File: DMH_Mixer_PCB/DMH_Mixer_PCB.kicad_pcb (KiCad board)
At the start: 2 copper layers, 48 x 138 mm, 41 parts, among them J0 Conn_01x01, J100 IDC_02x05, J200 IDC_02x05, J50 Conn_01x08, J60 Conn_01x08, SW1 SW_SPDT_321, SW2 SW_SPDT_321, SW3 SW_SPDT_321, SW4 SW_SPDT_321, U1 TL074

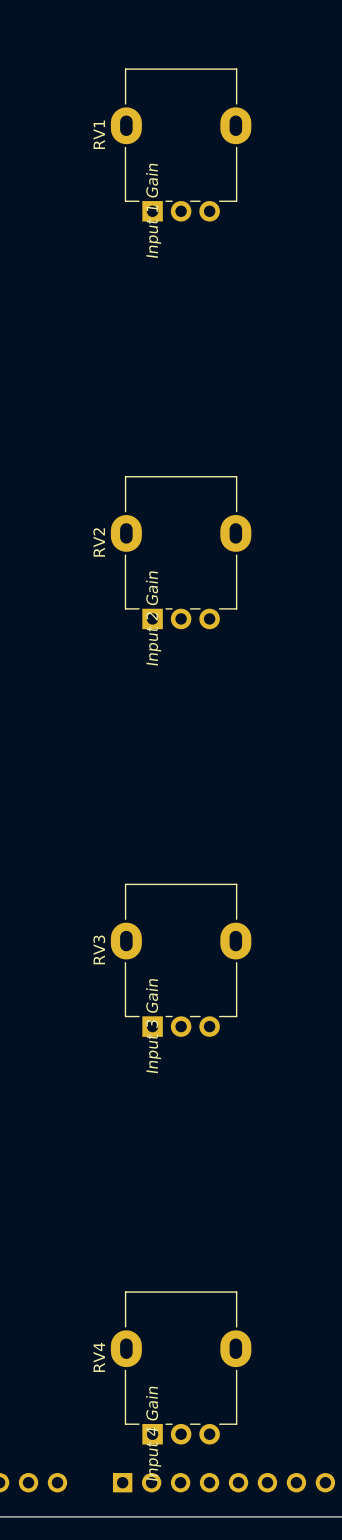
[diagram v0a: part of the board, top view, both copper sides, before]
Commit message: Moved pots to X=83,25
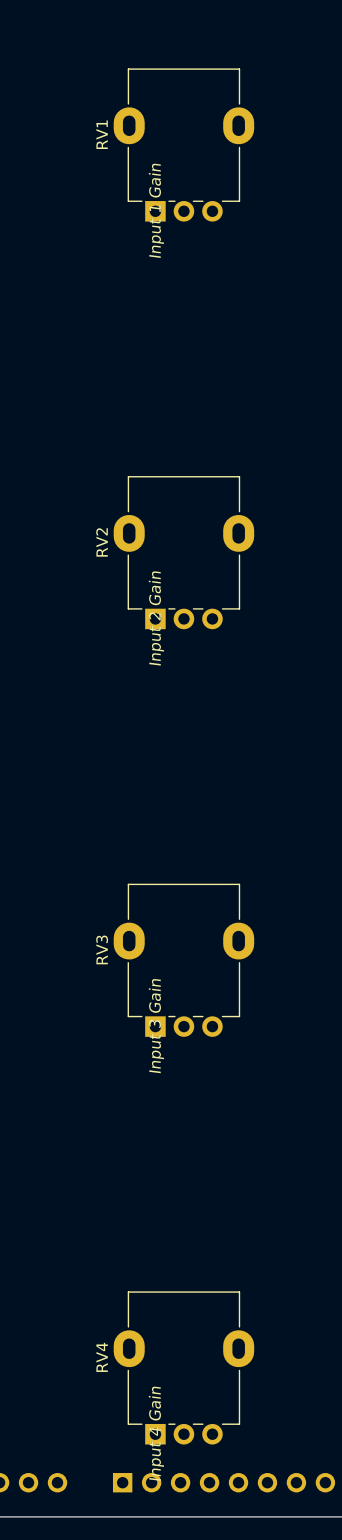
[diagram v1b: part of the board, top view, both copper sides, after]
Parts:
- moved RV1 0.25 mm to (80.8, 66.0)
- moved RV2 0.25 mm to (80.8, 101.8)
- moved RV3 0.25 mm to (80.8, 137.5)
- moved RV4 0.25 mm to (80.8, 173.2)
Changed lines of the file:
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@@
 	(footprint "SynthStuff:Potentiometer_Alpha_RD901F-40-00D_Single_Vertical"
 		(layer "F.Cu")
-		(at 80.5 173.25 90)
+		(at 80.75 173.25 90)
 		(descr "Potentiometer, vertical, 9mm, single, http://www.taiwanalpha.com.tw/downloads?target=products&id=113")
 		(tags "potentiometer vertical 9mm single")
@@
 	(footprint "SynthStuff:Potentiometer_Alpha_RD901F-40-00D_Single_Vertical"
 		(layer "F.Cu")
-		(at 80.5 101.75 90)
+		(at 80.75 101.75 90)
 		(descr "Potentiometer, vertical, 9mm, single, http://www.taiwanalpha.com.tw/downloads?target=products&id=113")
 		(tags "potentiometer vertical 9mm single")
@@
 	(footprint "SynthStuff:Potentiometer_Alpha_RD901F-40-00D_Single_Vertical"
 		(layer "F.Cu")
-		(at 80.5 137.5 90)
+		(at 80.75 137.5 90)
 		(descr "Potentiometer, vertical, 9mm, single, http://www.taiwanalpha.com.tw/downloads?target=products&id=113")
 		(tags "potentiometer vertical 9mm single")
@@
 	(footprint "SynthStuff:Potentiometer_Alpha_RD901F-40-00D_Single_Vertical"
 		(layer "F.Cu")
-		(at 80.5 66 90)
+		(at 80.75 66 90)
 		(descr "Potentiometer, vertical, 9mm, single, http://www.taiwanalpha.com.tw/downloads?target=products&id=113")
 		(tags "potentiometer vertical 9mm single")
@@
 	)
 	(gr_line
-		(start 83 169.25)
-		(end 83 162.25)
-		(stroke
-			(width 0.1)
-			(type default)
-		)
-		(layer "Cmts.User")
-	)
-	(gr_line
-		(start 79.5 58.5)
-		(end 86.5 58.5)
+		(start 83.25 169.25)
+		(end 83.25 162.25)
 		(stroke
 			(width 0.1)
@@
 	)
 	(gr_line
-		(start 79.5 94.25)
-		(end 86.5 94.25)
-		(stroke
-			(width 0.1)
-			(type default)
-		)
-		(layer "Cmts.User")
-	)
-	(gr_line
-		(start 83 62)
-		(end 83 55)
+		(start 79.75 94.25)
+		(end 86.75 94.25)
 		(stroke
 			(width 0.1)
@@
 	)
 	(gr_circle
-		(center 83 165.75)
-		(end 83 169.25)
+		(center 83.25 165.75)
+		(end 83.25 169.25)
 		(stroke
 			(width 0.1)
@@
 	)
 	(gr_line
-		(start 79.5 165.75)
-		(end 86.5 165.75)
+		(start 79.75 165.75)
+		(end 86.75 165.75)
 		(stroke
 			(width 0.1)
@@
 	)
 	(gr_line
-		(start 79.5 130)
-		(end 86.5 130)
+		(start 79.75 130)
+		(end 86.75 130)
 		(stroke
 			(width 0.1)
@@
 		(layer "Cmts.User")
 	)
+	(gr_line
+		(start 79.75 58.5)
+		(end 86.75 58.5)
+		(stroke
+			(width 0.1)
+			(type default)
+		)
+		(layer "Cmts.User")
+	)
 	(gr_circle
-		(center 83 130)
-		(end 83 133.5)
+		(center 83.25 130)
+		(end 83.25 133.5)
 		(stroke
 			(width 0.1)
@@
 	)
 	(gr_circle
-		(center 83 58.5)
-		(end 83 62)
+		(center 83.25 58.5)
+		(end 83.25 62)
 		(stroke
 			(width 0.1)
@@
 	)
 	(gr_line
-		(start 83 97.75)
-		(end 83 90.75)
+		(start 83.25 97.75)
+		(end 83.25 90.75)
 		(stroke
 			(width 0.1)
@@
 	)
 	(gr_circle
-		(center 83 94.25)
-		(end 83 97.75)
+		(center 83.25 94.25)
+		(end 83.25 97.75)
 		(stroke
 			(width 0.1)
@@
 	)
 	(gr_line
-		(start 83 133.5)
-		(end 83 126.5)
+		(start 83.25 62)
+		(end 83.25 55)
+		(stroke
+			(width 0.1)
+			(type default)
+		)
+		(layer "Cmts.User")
+	)
+	(gr_line
+		(start 83.25 133.5)
+		(end 83.25 126.5)
 		(stroke
 			(width 0.1)

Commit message: Component placement done
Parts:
- added C10: 1uF, Capacitor_THT:C_Disc_D4.3mm_W1.9mm_P5.00mm, B.Cu at (53.0, 158.5)
- added C7: 1uF, Capacitor_THT:C_Disc_D4.3mm_W1.9mm_P5.00mm, B.Cu at (53.0, 51.0)
- added C8: 1uF, Capacitor_THT:C_Disc_D4.3mm_W1.9mm_P5.00mm, B.Cu at (53.0, 86.8)
- added C9: 1uF, Capacitor_THT:C_Disc_D4.3mm_W1.9mm_P5.00mm, B.Cu at (53.0, 124.0)
- added R17: 100k, Resistor_THT:R_Axial_DIN0207_L6.3mm_D2.5mm_P7.62mm_Horizontal, B.Cu at (53.0, 65.8)
- added R18: 27k, Resistor_THT:R_Axial_DIN0207_L6.3mm_D2.5mm_P7.62mm_Horizontal, B.Cu at (53.0, 93.9)
- added R19: 100k, Resistor_THT:R_Axial_DIN0207_L6.3mm_D2.5mm_P7.62mm_Horizontal, B.Cu at (53.0, 138.8)
- added R20: 1k, Resistor_THT:R_Axial_DIN0207_L6.3mm_D2.5mm_P7.62mm_Horizontal, B.Cu at (53.0, 173.3)
- C1, C2, C3, C4, C5, C6, D1, D2, D4, D5, J100, J200, R1, R10, R3, R5, R9, U1: moved to B.Cu
- R11: value 27k -> 100k; moved to B.Cu
- R12, R7: value 1k -> 100k; moved to B.Cu
- R13, R14, R15: value 33k -> 100k; moved to B.Cu
- R16: value 33k -> 1k; moved to B.Cu
- R2, R4, R6, R8: value 100k -> 27k; moved to B.Cu
- moved J0 137.0 mm to (56.2, 155.2)
- moved SW4 123.5 mm to (58.5, 165.8)
- moved C1 119.8 mm to (73.0, 47.2), turned to 180 degrees
- moved D5 106.1 mm to (77.4, 46.0)
- moved J200 105.3 mm to (70.3, 158.3), turned to 180 degrees
- moved C3 103.6 mm to (72.9, 110.2), turned to -90 degrees
- moved C4 102.7 mm to (82.1, 50.6), turned to 180 degrees
- moved RV5 100.6 mm to (53.9, 113.5), turned to 90 degrees
- moved SW3 97.1 mm to (58.5, 130.0)
- moved C2 90.8 mm to (94.5, 82.2)
- moved D1 89.4 mm to (59.4, 109.5)
- moved C5 85.8 mm to (91.2, 78.7), turned to 90 degrees
- moved D2 81.5 mm to (67.1, 115.2), turned to 180 degrees
- moved D4 81.2 mm to (95.8, 65.9), turned to -90 degrees
- moved C6 81.1 mm to (94.2, 110.2), turned to -90 degrees
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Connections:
- R1 pad 1: Net-(SW1-C) -> Net-(SW1-A)
- R10 pad 1: Net-(U1C--) -> GND
- R10 pad 2: Net-(R10-Pad2) -> Net-(C8-Pad2)
- R11 pad 2: Net-(U1C--) -> Net-(C9-Pad2)
- R12 pad 1: Net-(R10-Pad2) -> GND
- R12 pad 2: /Core Circuit/Clipped Output -> Net-(C10-Pad2)
- R13 pad 1: Net-(SW1-B) -> Net-(U1A--)
- R13 pad 2: Net-(U1A--) -> Net-(R13-Pad2)
- R14 pad 1: Net-(SW2-B) -> Net-(R13-Pad2)
- R14 pad 2: Net-(U1A--) -> Net-(U1B--)
- R15 pad 1: Net-(SW3-B) -> Net-(U1B--)
- R15 pad 2: Net-(U1A--) -> Net-(U1D-+)
- R16 pad 1: Net-(SW4-B) -> Net-(U1D--)
- R16 pad 2: Net-(U1A--) -> /Core Circuit/Output
- R2 pad 1: Net-(SW2-C) -> Net-(C7-Pad2)
- R3 pad 1: Net-(SW3-C) -> Net-(SW2-A)
- R4 pad 1: Net-(U1A--) -> Net-(C8-Pad2)
- R4 pad 2: Net-(R4-Pad2) -> Net-(U1A--)
- R5 pad 1: Net-(R4-Pad2) -> Net-(SW3-A)
- R5 pad 2: Net-(U1B--) -> Net-(U1A--)
- R6 pad 1: Net-(U1B--) -> Net-(C9-Pad2)
- R6 pad 2: Net-(U1D-+) -> Net-(U1A--)
- R7 pad 1: Net-(U1D--) -> Net-(SW4-A)
- R7 pad 2: /Core Circuit/Output -> Net-(U1A--)
- R8 pad 1: Net-(SW4-C) -> Net-(C10-Pad2)
- R9 pad 1: Net-(U1D-+) -> GND
- R9 pad 2: Net-(D1-A) -> Net-(C7-Pad2)
- RV1 pad 2: Net-(SW1-C) -> Net-(SW1-B)
- RV2 pad 2: Net-(SW2-C) -> Net-(SW2-B)
- RV3 pad 2: Net-(SW3-C) -> Net-(SW3-B)
- RV4 pad 2: Net-(SW4-C) -> Net-(SW4-B)
- SW1 pad 3: unconnected-(SW1-A-Pad3) -> Net-(SW1-A)
- SW2 pad 3: unconnected-(SW2-A-Pad3) -> Net-(SW2-A)
- SW3 pad 3: unconnected-(SW3-A-Pad3) -> Net-(SW3-A)
- SW4 pad 3: unconnected-(SW4-A-Pad3) -> Net-(SW4-A)
- U1 pad 1: Net-(R4-Pad2) -> Net-(R13-Pad2)
- U1 pad 8: Net-(R10-Pad2) -> Net-(R19-Pad2)

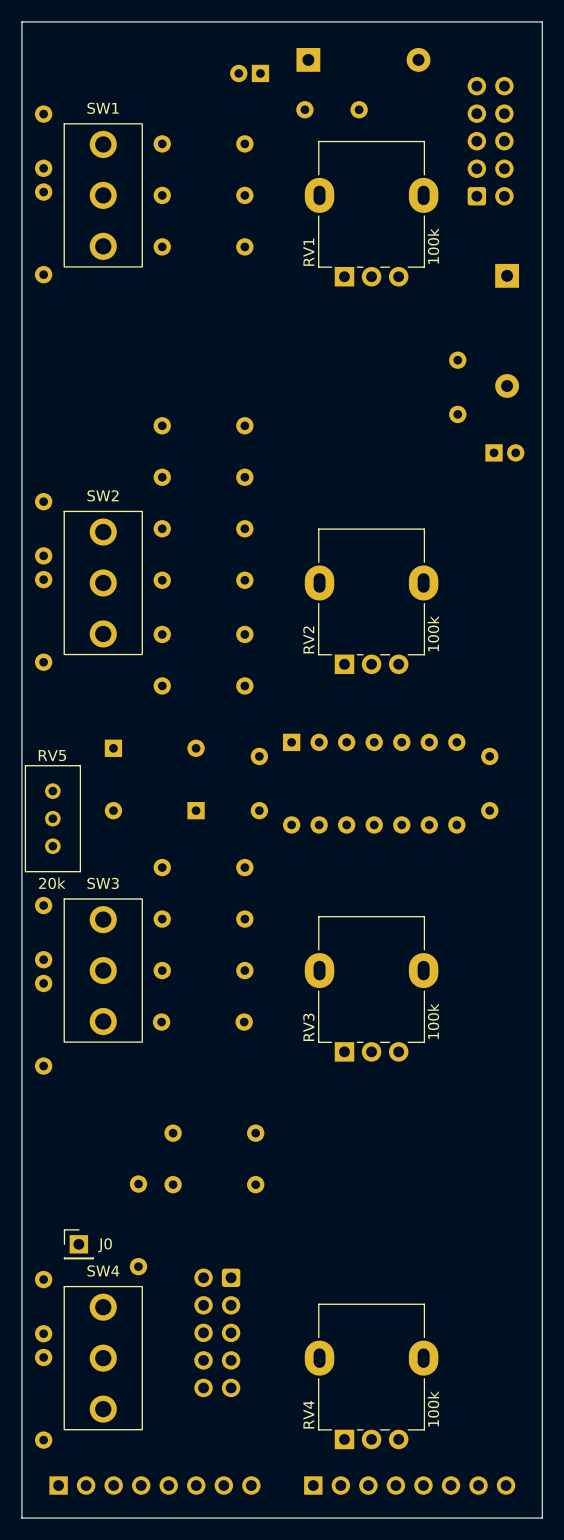
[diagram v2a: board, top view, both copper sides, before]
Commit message: ReRouted PCB
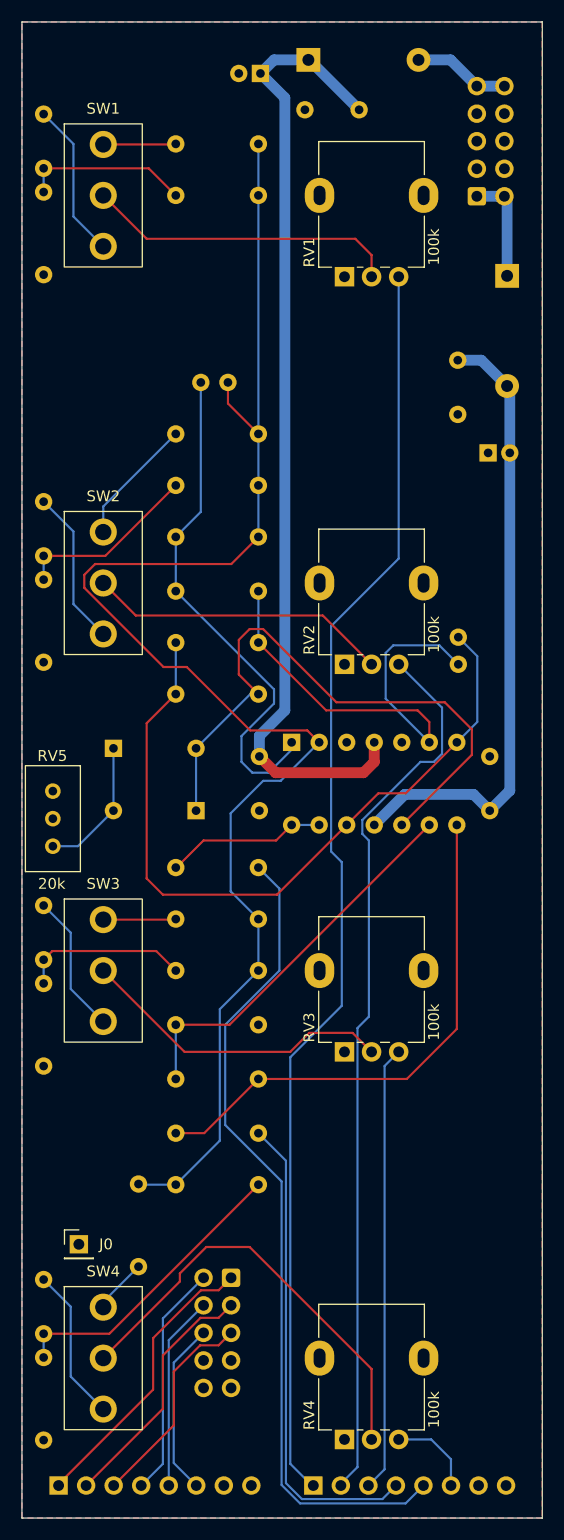
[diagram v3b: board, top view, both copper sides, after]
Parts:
- added C11: 47pF, Capacitor_THT:C_Disc_D3.0mm_W2.0mm_P2.50mm, B.Cu at (70.0, 75.8)
- added C12: 47pF, Capacitor_THT:C_Disc_D3.0mm_W2.0mm_P2.50mm, B.Cu at (91.2, 101.8)
- moved R18 45.6 mm to (72.8, 135.0), turned to 180 degrees
- moved R17 40.6 mm to (65.2, 104.5), turned to 0 degrees
- moved R20 30.8 mm to (65.2, 145.0), turned to 0 degrees
- moved R12 30.7 mm to (53.0, 173.3), turned to 90 degrees
- moved R10 28.6 mm to (53.0, 101.6), turned to 90 degrees
- moved R11 18.9 mm to (53.0, 138.8), turned to 90 degrees
- moved R9 18.7 mm to (53.0, 65.8), turned to 90 degrees
- moved R19 12.2 mm to (65.2, 140.0), turned to 0 degrees
- moved R13 4.19 mm to (72.8, 90.0)
- moved R14 4.19 mm to (65.2, 95.0)
- moved R15 4.19 mm to (72.8, 99.8)
- moved R3 4.19 mm to (65.2, 80.5)
- moved R4 4.19 mm to (65.2, 85.2)
- moved R1 1.25 mm to (65.2, 53.8)
- moved R16 1.25 mm to (65.2, 120.5)
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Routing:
- net Net-(U1A--): track 0.00 -> 141.2 mm
- net /Core Circuit/Input 1: track 0.00 -> 117.4 mm
- net +12V: track 0.00 -> 89.9 mm
- net /Core Circuit/Input 2: track 0.00 -> 82.5 mm
- net /Core Circuit/Output: track 0.00 -> 76.5 mm
- net Net-(U1D-+): track 0.00 -> 69.1 mm
- net -12V: track 0.00 -> 58.0 mm
- net Net-(D1-A): track 0.00 -> 56.6 mm
- net Net-(R19-Pad2): track 0.00 -> 48.7 mm
- net Net-(C11-Pad2): track 0.00 -> 47.5 mm
- net /Core Circuit/Clipped Output: track 0.00 -> 44.6 mm
- net Net-(U1B--): track 0.00 -> 43.1 mm
- net /Core Circuit/Input 3: track 0.00 -> 41.2 mm
- net Net-(SW4-B): track 0.00 -> 40.6 mm
- net Net-(U1C--): track 0.00 -> 36.0 mm
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- added copper zone on B.Cu, net GND
- added copper zone on F.Cu, net GND

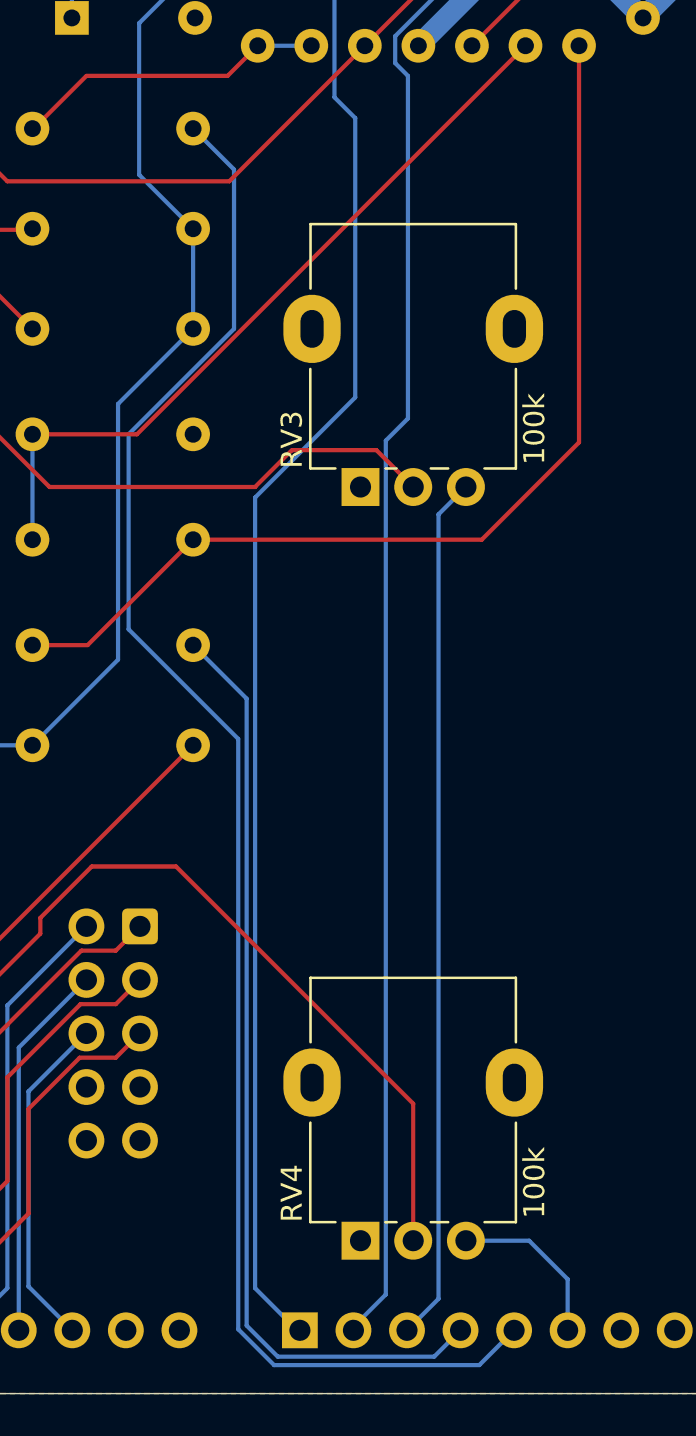
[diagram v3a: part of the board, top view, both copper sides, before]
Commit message: Moved output jacks to bottom right
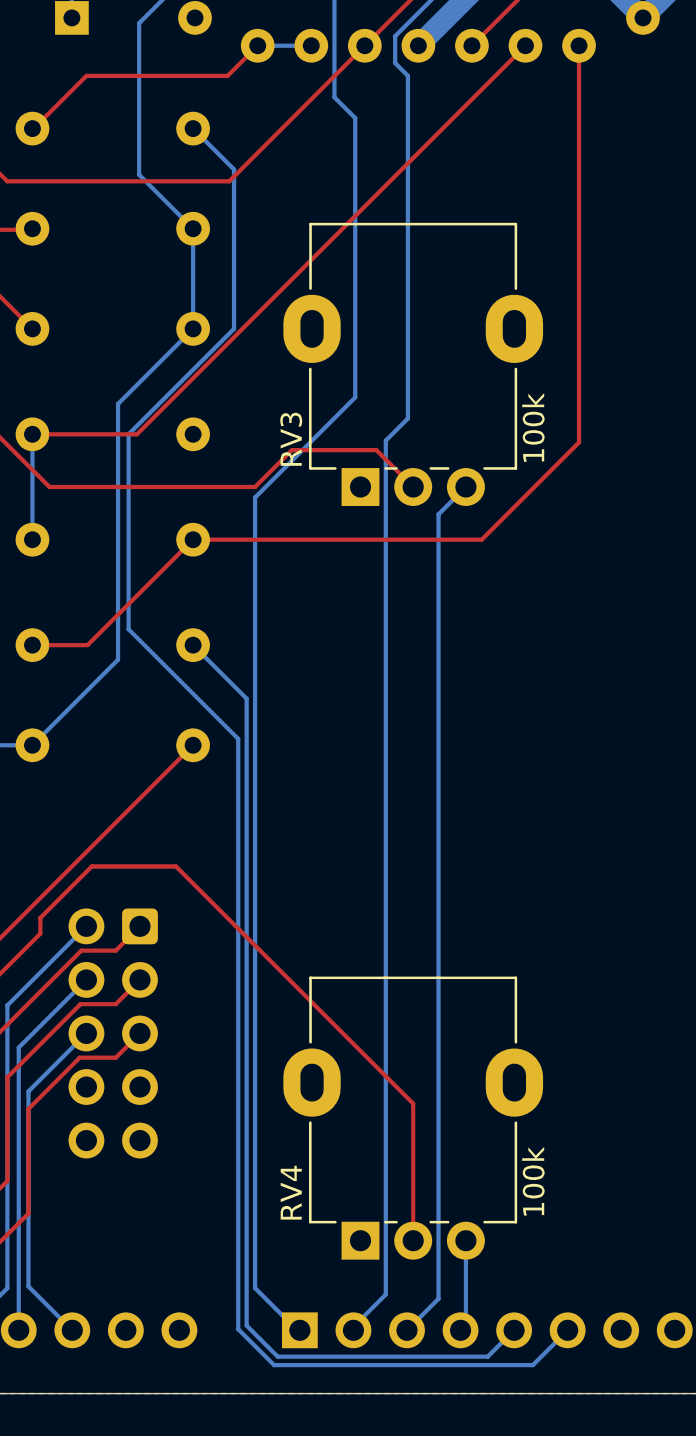
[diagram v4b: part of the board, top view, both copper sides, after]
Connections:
- J50 pad 4: /Core Circuit/Clipped Output -> /Core Circuit/Input 4
- J50 pad 5: /Core Circuit/Output -> /Core Circuit/Clipped Output
- J50 pad 6: /Core Circuit/Input 4 -> /Core Circuit/Output
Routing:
- net /Core Circuit/Input 4: track 8.01 -> 4.36 mm
- net /Core Circuit/Output: track 76.5 -> 79.0 mm
- net /Core Circuit/Clipped Output: track 44.6 -> 47.1 mm
